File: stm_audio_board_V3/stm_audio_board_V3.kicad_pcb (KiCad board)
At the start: 4 copper layers, 201 x 117 mm, 258 parts, among them J1 Power conn, J10 USB_A, J11 AudioJack_Loop1_Return, J12 AudioJack_Loop1_Send, J13 AudioJack_INPUT_Main, J14 AudioJack_OUTPUT_Main, J15 AudioJack_Loop2_Send, J16 STlink_DISP_MCU, J2 STlink_DSP, J3 Audio_sig, J4 Conn_01x01_taptempo, J5 Barrel_Jack_MountingPin, J6 Conn_01x03_pot_ext, J7 AudioJack_Loop3_Return, J8 AudioJack_Loop3_Send, J9 AudioJack_Loop2_Return, SW1 SW_SPST, SW2 SW_SPST, U1 IS42S16100H-7TL, U10 OP275, U12 OP275, U13 LM7809_TO220, U14 OP275, U15 STM32H723ZGTx, U16 LM7909_TO220, U2 OP275, U3 R-78B5.0-2.0, U4 OP275, U5 MIC2920A-3.3WS-TR, U7 STM32H723ZGTx, U8 OP275, U9 MIC2920A-3.3WS-TR, Y1 X1E0000210132, Y2 X1E0000210132

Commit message: isolated power section done
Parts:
- removed C104, C105: 2u2F, Capacitor_SMD:C_0805_2012Metric_Pad1.18x1.45mm_HandSolder
- removed C132: 100uF, Capacitor_THT:CP_Radial_D6.3mm_P2.50mm
- removed D1: 1N4148, Diode_SMD:D_1206_3216Metric_Pad1.42x1.75mm_HandSolder
- removed FB4: TDK MMZ1608R601ATD25 DB, Resistor_SMD:R_0603_1608Metric_Pad0.98x0.95mm_HandSolder
- removed U3: R-78B5.0-2.0, Converter_DCDC:Converter_DCDC_RECOM_R-78B-2.0_THT
- added C103: 4.7uF, Capacitor_THT:CP_Radial_D6.3mm_P2.50mm, F.Cu at (295.6, 119.4)
- added C138: 100uF, Capacitor_THT:CP_Radial_D6.3mm_P2.50mm, F.Cu at (261.3, 108.5)
- added C139: 100uF, Capacitor_THT:CP_Radial_D6.3mm_P2.50mm, F.Cu at (253.0, 108.4)
- added C140: 47uF, Capacitor_THT:CP_Radial_D6.3mm_P2.50mm, F.Cu at (258.5, 140.5)
- added C48: 100uF, Capacitor_THT:CP_Radial_D6.3mm_P2.50mm, F.Cu at (288.9, 131.6)
- added C69: 100uF, Capacitor_THT:CP_Radial_D6.3mm_P2.50mm, F.Cu at (279.2, 131.4)
- added C75: 100uF, Capacitor_THT:CP_Radial_D6.3mm_P2.50mm, F.Cu at (300.9, 141.1)
- added C76: 100uF, Capacitor_THT:CP_Radial_D6.3mm_P2.50mm, F.Cu at (277.3, 140.6)
- added C77: 100uF, Capacitor_THT:CP_Radial_D6.3mm_P2.50mm, F.Cu at (269.3, 140.6)
- added L4: 10uH, Inductor_SMD:L_6.3x6.3_H3, F.Cu at (286.3, 142.1)
- added L5: 10uH, Inductor_SMD:L_6.3x6.3_H3, F.Cu at (238.2, 113.8)
- added PS1: URB2405S-6WR3, Converter_DCDC:Converter_DCDC_XP_POWER-ITxxxxxS_THT, F.Cu at (271.4, 132.4)
- C13: value 22uF 50V poly -> 100uF; footprint Capacitor_THT:CP_Radial_D5.0mm_P2.00mm -> Capacitor_THT:CP_Radial_D6.3mm_P2.50mm
- C133: value 47uF -> 4.7uF
- C15: value 2u2F -> 100uF; footprint Capacitor_SMD:C_0805_2012Metric_Pad1.18x1.45mm_HandSolder -> Capacitor_THT:CP_Radial_D6.3mm_P2.50mm
- C27: value 100n -> 100uF; footprint Capacitor_SMD:C_0603_1608Metric -> Capacitor_THT:CP_Radial_D6.3mm_P2.50mm
- C4: value 22uF tantal -> 100uF; footprint Capacitor_Tantalum_SMD:CP_EIA-7343-31_Kemet-D_Pad2.25x2.55mm_HandSolder -> Capacitor_THT:CP_Radial_D6.3mm_P2.50mm
- moved C9 44.3 mm to (194.4, 122.0), turned to 90 degrees
- moved C8 39.9 mm to (194.4, 113.9), turned to 90 degrees
- moved C13 39.3 mm to (293.9, 141.2), turned to -90 degrees
- moved J5 36.2 mm to (297.8, 132.7)
- moved C89 33.3 mm to (204.8, 70.7), turned to 0 degrees
- moved C27 31.9 mm to (254.4, 85.6), turned to 180 degrees
- moved C28 28.8 mm to (261.9, 85.6), turned to 0 degrees
- moved L1 23.7 mm to (287.3, 120.1), turned to 180 degrees
- moved C133 21.9 mm to (278.9, 119.3)
- moved C15 21.4 mm to (234.4, 104.4)
- moved C30 20.9 mm to (209.8, 87.0)
- moved C102 19.0 mm to (243.0, 113.1), turned to 0 degrees
- moved C4 17.9 mm to (245.4, 116.6), turned to -90 degrees
- moved C70 15.6 mm to (241.2, 126.1), turned to -90 degrees
- moved C119 14.4 mm to (260.8, 56.4), turned to 0 degrees
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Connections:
- C13 pad 2: GND -> Earth
- C133 pad 2: GND -> Earth
- C15 pad 1: 5V -> Net-(U5-VI)
- C27 pad 1: Net-(U5-VI) -> GND
- C27 pad 2: GND -> -9V
- C28 pad 1: Net-(U5-VI) -> +9V
- J5 pad 2: GND -> Earth
- PS2 pad 1: GND -> Earth
- U13 pad 3: unconnected-(U13-VO-Pad3) -> +9V
- U16 pad 3: unconnected-(U16-VO-Pad3) -> -9V
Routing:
- net +9V: track 245.3 -> 196.8 mm, vias 6 -> 5
- net ADC1N: track 43.5 -> 6.32 mm
- net ADC1P: track 43.1 -> 6.15 mm
- net GND: track 90.7 -> 117.4 mm
- net AD1939_CM: track 216.2 -> 197.1 mm, vias 12 -> 10
- net Audio_Main_Input: track 12.2 -> 6.80 mm
- added copper zone on In1.Cu, net Earth
- added copper zone on In2.Cu, net Earth
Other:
- board size 201 x 117 mm -> 236.9 x 117.5 mm

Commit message: minor power section fixes
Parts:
- added C104: 10uF, Capacitor_SMD:C_1206_3216Metric, F.Cu at (285.7, 142.7)
- added C105: 10uF, Capacitor_SMD:C_1206_3216Metric, F.Cu at (283.1, 142.7)
- added C132: 10uF, Capacitor_SMD:C_1206_3216Metric, F.Cu at (272.6, 142.7)
- added C136: 10uF, Capacitor_SMD:C_1206_3216Metric, F.Cu at (270.0, 142.7)
- added C137: 10uF, Capacitor_SMD:C_1206_3216Metric, F.Cu at (286.3, 119.1)
- added C141: 10uF, Capacitor_SMD:C_1206_3216Metric, F.Cu at (324.3, 105.5)
- added C142: 10uF, Capacitor_SMD:C_1206_3216Metric, F.Cu at (324.3, 108.9)
- added C143: 10uF, Capacitor_SMD:C_1206_3216Metric, F.Cu at (324.3, 112.2)
- added C144: 10uF, Capacitor_SMD:C_1206_3216Metric, F.Cu at (329.9, 95.5)
- added C145: 10uF, Capacitor_SMD:C_1206_3216Metric, F.Cu at (329.9, 98.8)
- added C146: 10uF, Capacitor_SMD:C_1206_3216Metric, F.Cu at (329.9, 102.2)
- added C147: 10uF, Capacitor_SMD:C_1206_3216Metric, F.Cu at (329.9, 105.5)
- added C148: 10uF, Capacitor_SMD:C_1206_3216Metric, F.Cu at (237.3, 142.0)
- added C149: 10uF, Capacitor_SMD:C_1206_3216Metric, F.Cu at (242.7, 142.1)
- added C150: 100uF, Capacitor_THT:CP_Radial_D6.3mm_P2.50mm, F.Cu at (232.0, 128.9)
- added C151: 100uF, Capacitor_THT:CP_Radial_D6.3mm_P2.50mm, F.Cu at (232.1, 143.2)
- added C152: 10uF, Capacitor_SMD:C_1206_3216Metric, F.Cu at (322.6, 89.8)
- added C153: 10uF, Capacitor_SMD:C_1206_3216Metric, F.Cu at (322.6, 93.1)
- added C154: 10uF, Capacitor_SMD:C_1206_3216Metric, F.Cu at (322.6, 96.5)
- added C155: 10uF, Capacitor_SMD:C_1206_3216Metric, F.Cu at (322.6, 99.8)
- added L6: 10uH, Inductor_SMD:L_6.3x6.3_H3, F.Cu at (239.9, 136.0)
- C103, C133: value 4.7uF -> 10uF; footprint Capacitor_THT:CP_Radial_D6.3mm_P2.50mm -> Capacitor_SMD:C_1206_3216Metric
- C138, C139: value 100uF -> 10uF; footprint Capacitor_THT:CP_Radial_D6.3mm_P2.50mm -> Capacitor_SMD:C_1206_3216Metric
- C140: value 47uF -> 100uF
- moved C139 71.5 mm to (324.3, 102.2)
- moved H4 54.9 mm to (291.8, 71.6)
- moved C140 26.9 mm to (232.0, 136.0)
- moved C75 21.7 mm to (284.3, 127.2), turned to 90 degrees
- moved C4 17.9 mm to (237.9, 100.3)
- moved L5 17.9 mm to (230.7, 97.5)
- moved C13 17.6 mm to (279.8, 130.6), turned to 180 degrees
- moved C70 16.7 mm to (229.7, 114.0)
- moved C15 16.5 mm to (237.1, 88.1)
- moved C29 15.4 mm to (237.7, 79.5)
- moved C138 13.7 mm to (272.2, 116.8), turned to -90 degrees
- moved C76 13.6 mm to (269.7, 129.4), turned to 90 degrees
- moved C77 13.5 mm to (261.8, 129.4), turned to 90 degrees
- moved C103 12.1 mm to (283.5, 119.1), turned to 90 degrees
- moved C102 11.3 mm to (233.8, 106.6)
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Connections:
- C138 pad 1: Net-(U13-VI) -> Net-(PS2-+Vin)
- C138 pad 2: GND -> Earth
- C139 pad 1: GND -> Net-(U16-VI)
- C139 pad 2: Net-(U16-VI) -> GND
- PS1 pad 6: 5V -> Net-(PS1-+Vout)
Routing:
- net 5V: track 0.00 -> 32.3 mm
- net PWR_INPUT_12V-18V: track 0.00 -> 19.1 mm
- net Net-(PS1-+Vout): track 0.00 -> 16.3 mm
- net Net-(PS2-+Vin): track 0.00 -> 15.9 mm
- net Net-(PS1-+Vin): track 0.00 -> 9.46 mm
- net Earth: vias 0 -> 25
- added copper zone on F.Cu, net Earth
- added copper zone on F.Cu, net Net-(PS1-+Vin)
- added copper zone on F.Cu, net PWR_INPUT_12V-18V
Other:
- board size 236.9 x 117.5 mm -> 230.9 x 117 mm

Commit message: safety commit
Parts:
- moved C145 81.8 mm to (249.2, 86.1), turned to 180 degrees
- moved C144 81.0 mm to (249.2, 88.6), turned to 180 degrees
- moved C141 80.5 mm to (243.8, 105.9), turned to -90 degrees
- moved C139 78.0 mm to (246.4, 105.9), turned to -90 degrees
- moved C154 74.4 mm to (248.9, 105.9), turned to -90 degrees
- moved C147 70.4 mm to (261.5, 88.7)
- moved C146 70.2 mm to (261.5, 86.3)
- moved C155 69.1 mm to (254.4, 88.6)
- moved C143 59.3 mm to (265.3, 106.0), turned to -90 degrees
- moved C142 56.5 mm to (267.8, 106.0), turned to -90 degrees
- moved C153 56.2 mm to (266.6, 88.7), turned to 180 degrees
- moved C152 54.7 mm to (270.3, 106.0), turned to -90 degrees
- moved C27 4.70 mm to (254.3, 80.9)
- moved C28 4.65 mm to (261.2, 81.0)
- moved C134 0.22 mm to (269.3, 99.8)
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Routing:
- net Net-(U16-VI): track 0.00 -> 26.3 mm
- net Net-(U13-VI): track 0.00 -> 25.9 mm
- net /Power/-12V: track 0.00 -> 23.6 mm
- net /Power/+12V: track 0.00 -> 22.8 mm
- net GND: track 117.4 -> 133.7 mm, vias 56 -> 85
- net -9V: track 225.8 -> 237.0 mm
- net +9V: track 196.8 -> 206.1 mm
- added copper zone on F.Cu, net GND
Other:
- board text added: "POWER INPUT 18V"

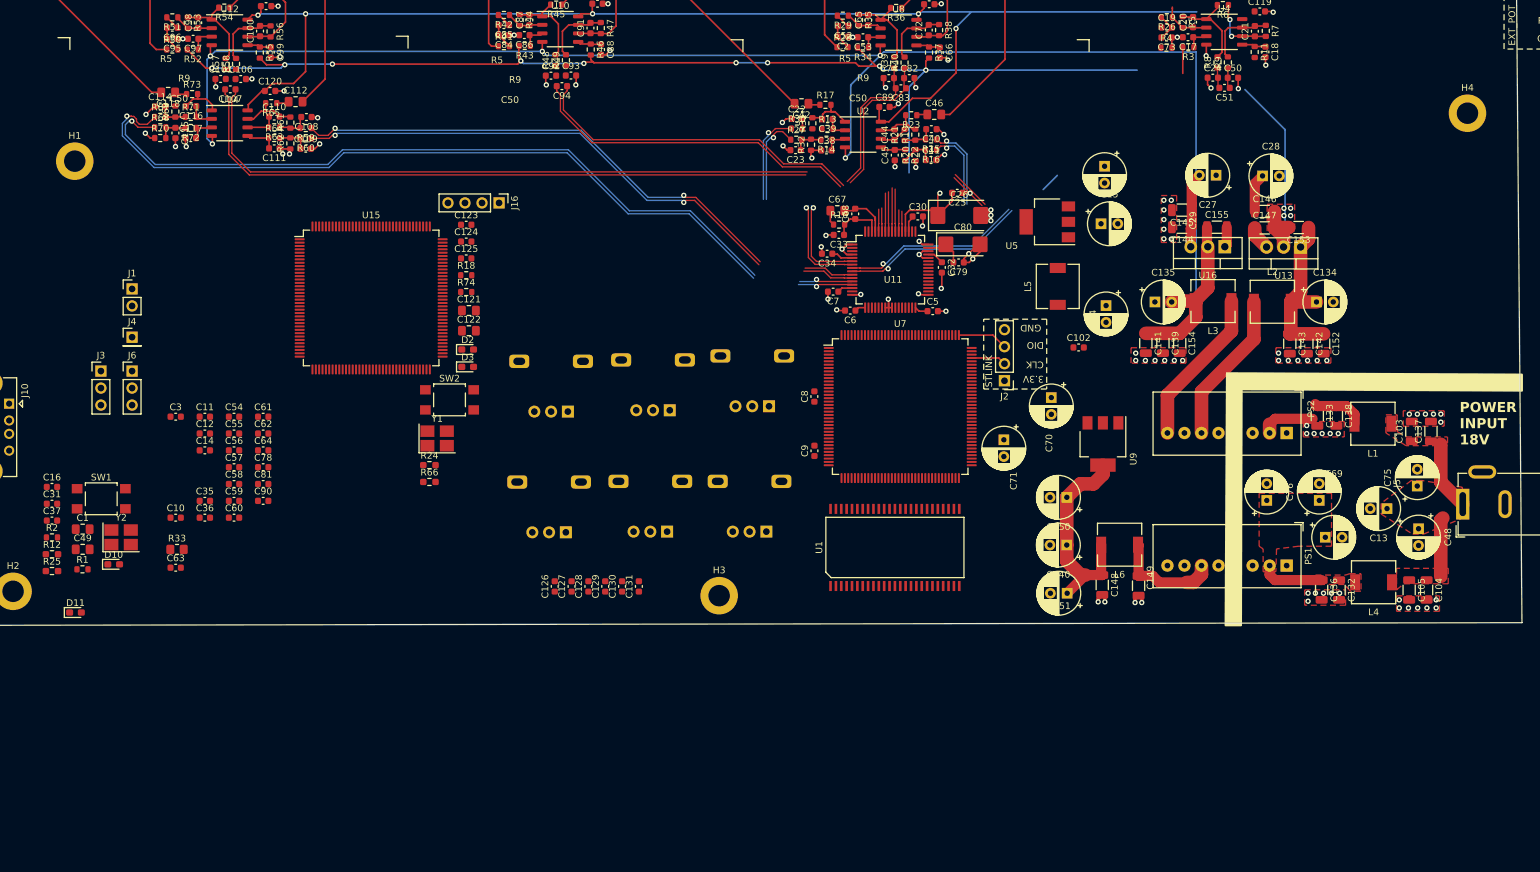
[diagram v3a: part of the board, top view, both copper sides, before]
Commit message: Analog power and SDRAm routing reworked
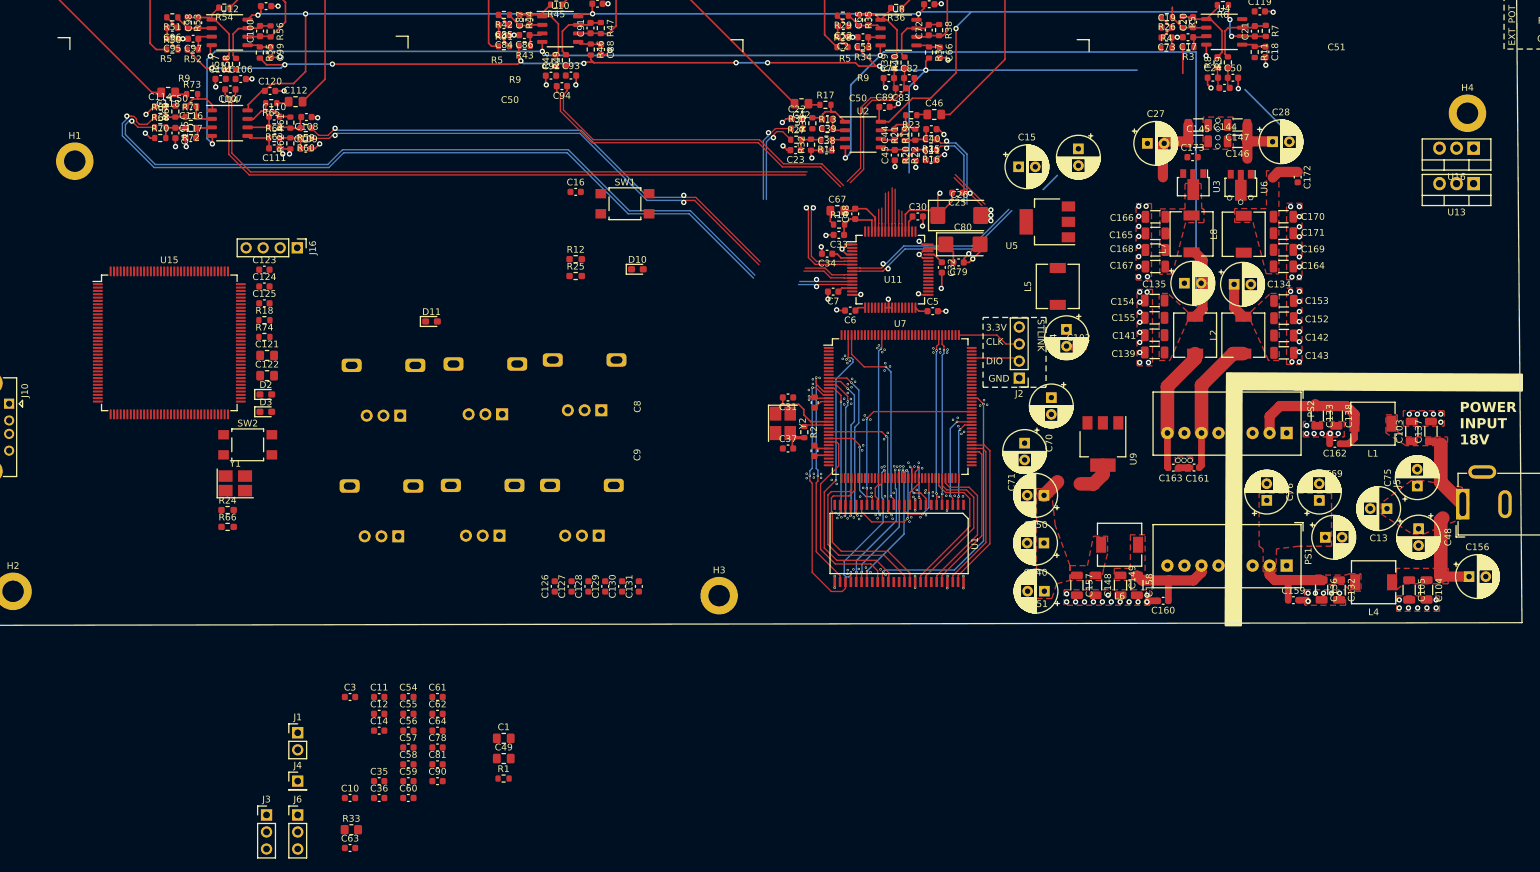
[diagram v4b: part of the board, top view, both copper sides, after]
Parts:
- added C156: 100uF, Capacitor_THT:CP_Radial_D6.3mm_P2.50mm, F.Cu at (292.0, 140.7)
- added C157: 10uF, Capacitor_SMD:C_1206_3216Metric, F.Cu at (233.5, 142.0)
- added C158: 10uF, Capacitor_SMD:C_1206_3216Metric, F.Cu at (242.5, 142.0)
- added C159: 100nF, Capacitor_SMD:C_0603_1608Metric, F.Cu at (265.8, 144.2)
- added C160: 100nF, Capacitor_SMD:C_0603_1608Metric, F.Cu at (246.4, 144.3)
- added C161: 100nF, Capacitor_SMD:C_0603_1608Metric, F.Cu at (251.0, 124.5)
- added C162: 100nF, Capacitor_SMD:C_0603_1608Metric, F.Cu at (272.0, 120.9)
- added C163: 100nF, Capacitor_SMD:C_0603_1608Metric, F.Cu at (247.9, 124.5)
- added C164: 10uF, Capacitor_SMD:C_1206_3216Metric, F.Cu at (264.3, 94.5)
- added C165: 10uF, Capacitor_SMD:C_1206_3216Metric, F.Cu at (245.2, 89.5)
- added C166: 10uF, Capacitor_SMD:C_1206_3216Metric, F.Cu at (245.2, 87.1)
- added C167: 10uF, Capacitor_SMD:C_1206_3216Metric, F.Cu at (245.2, 94.5)
- added C168: 10uF, Capacitor_SMD:C_1206_3216Metric, F.Cu at (245.2, 92.0)
- added C169: 10uF, Capacitor_SMD:C_1206_3216Metric, F.Cu at (264.3, 92.0)
- added C170: 10uF, Capacitor_SMD:C_1206_3216Metric, F.Cu at (264.3, 87.1)
- added C171: 10uF, Capacitor_SMD:C_1206_3216Metric, F.Cu at (264.3, 89.5)
- added C172: 100nF, Capacitor_SMD:C_0603_1608Metric, F.Cu at (266.5, 81.2)
- added C173: 100nF, Capacitor_SMD:C_0603_1608Metric, F.Cu at (250.8, 78.2)
- added L7: 10uH, Inductor_SMD:L_6.3x6.3_H3, F.Cu at (250.6, 89.6)
- added L8: 10uH, Inductor_SMD:L_6.3x6.3_H3, F.Cu at (258.4, 89.7)
- added U3: 7909, Package_TO_SOT_SMD:SOT-89-3, F.Cu at (250.9, 82.6)
- added U6: 7809, Package_TO_SOT_SMD:SOT-89-3, F.Cu at (258.0, 82.7)
- moved R2 113.3 mm to (192.9, 119.2), turned to -90 degrees
- moved C31 110.9 mm to (190.4, 114.0), turned to 180 degrees
- moved C37 110.3 mm to (190.4, 121.6)
- moved Y2 100.2 mm to (189.7, 117.9), turned to -90 degrees
- moved R12 89.6 mm to (158.8, 93.4)
- moved C16 89.6 mm to (158.8, 83.4)
- moved D10 89.6 mm to (168.0, 94.9)
- moved R25 89.6 mm to (158.8, 95.9)
- moved SW1 89.6 mm to (166.1, 85.1)
- moved J1 70.7 mm to (117.3, 164.0)
- moved J3 70.7 mm to (112.7, 176.3)
- moved J6 70.7 mm to (117.3, 176.3)
- moved J4 70.7 mm to (117.3, 171.2)
- moved C49 70.1 mm to (148.1, 167.9)
- moved C1 70.1 mm to (148.1, 164.9)
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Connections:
- C134 pad 1: Net-(U13-VI) -> Net-(C134-Pad1)
- C135 pad 2: Net-(U16-VI) -> Net-(C135-Pad2)
- C139 pad 1: Net-(U16-VI) -> Net-(C135-Pad2)
- C141 pad 1: Net-(U16-VI) -> Net-(C135-Pad2)
- C142 pad 1: Net-(U13-VI) -> Net-(C134-Pad1)
- C143 pad 1: Net-(U13-VI) -> Net-(C134-Pad1)
- C152 pad 1: Net-(U13-VI) -> Net-(C134-Pad1)
- C153 pad 1: Net-(U13-VI) -> Net-(C134-Pad1)
- C154 pad 1: Net-(U16-VI) -> Net-(C135-Pad2)
- C155 pad 1: Net-(U16-VI) -> Net-(C135-Pad2)
- L2 pad 2: Net-(U13-VI) -> Net-(C134-Pad1)
- L3 pad 2: Net-(U16-VI) -> Net-(C135-Pad2)
- U1 pad 1: unconnected-(U1B-VDD-Pad1) -> +3.3V
- U1 pad 10: unconnected-(U1B-GNDQ-Pad10) -> GND
- U1 pad 11: unconnected-(U1A-DQ6-Pad11) -> /MCU/DSP_SDRAM_DATA_BUS6
- U1 pad 12: unconnected-(U1A-DQ7-Pad12) -> /MCU/DSP_SDRAM_DATA_BUS7
- U1 pad 13: unconnected-(U1B-VDDQ-Pad13) -> +3.3V
- U1 pad 14: unconnected-(U1A-LDQM-Pad14) -> /MCU/DSP_SDRAM_LDQM
- U1 pad 15: unconnected-(U1A-/WE-Pad15) -> /MCU/DSP_SDRAM_WE
- U1 pad 16: unconnected-(U1A-/CAS-Pad16) -> /MCU/DSP_SDRAM_CAS
- U1 pad 17: unconnected-(U1A-/RAS-Pad17) -> /MCU/DSP_SDRAM_RAS
- U1 pad 18: unconnected-(U1A-/CS-Pad18) -> /MCU/DSP_SDRAM_CS
- U1 pad 19: unconnected-(U1A-A11-Pad19) -> /MCU/DSP_SDRAM_ADRESS_BUS11
- U1 pad 2: unconnected-(U1A-DQ0-Pad2) -> /MCU/DSP_SDRAM_DATA_BUS0
- U1 pad 20: unconnected-(U1A-A10-Pad20) -> /MCU/DSP_SDRAM_ADRESS_BUS10
- U1 pad 21: unconnected-(U1A-A0-Pad21) -> /MCU/DSP_SDRAM_ADRESS_BUS0
- U1 pad 22: unconnected-(U1A-A1-Pad22) -> /MCU/DSP_SDRAM_ADRESS_BUS1
- U1 pad 23: unconnected-(U1A-A2-Pad23) -> /MCU/DSP_SDRAM_ADRESS_BUS2
- U1 pad 24: unconnected-(U1A-A3-Pad24) -> /MCU/DSP_SDRAM_ADRESS_BUS3
- U1 pad 25: unconnected-(U1B-VDD-Pad25) -> +3.3V
- U1 pad 26: unconnected-(U1B-GND-Pad26) -> GND
- U1 pad 27: unconnected-(U1A-A4-Pad27) -> /MCU/DSP_SDRAM_ADRESS_BUS4
- U1 pad 28: unconnected-(U1A-A5-Pad28) -> /MCU/DSP_SDRAM_ADRESS_BUS5
- U1 pad 29: unconnected-(U1A-A6-Pad29) -> /MCU/DSP_SDRAM_ADRESS_BUS6
- U1 pad 3: unconnected-(U1A-DQ1-Pad3) -> /MCU/DSP_SDRAM_DATA_BUS1
- U1 pad 30: unconnected-(U1A-A7-Pad30) -> /MCU/DSP_SDRAM_ADRESS_BUS7
- U1 pad 31: unconnected-(U1A-A8-Pad31) -> /MCU/DSP_SDRAM_ADRESS_BUS8
- U1 pad 32: unconnected-(U1A-A9-Pad32) -> /MCU/DSP_SDRAM_ADRESS_BUS9
- U1 pad 34: unconnected-(U1A-CKE-Pad34) -> /MCU/DSP_SDRAM_CKE
- U1 pad 35: unconnected-(U1A-CLK-Pad35) -> /MCU/DSP_SDRAM_CLK
- U1 pad 36: unconnected-(U1A-UDQM-Pad36) -> /MCU/DSP_SDRAM_UDQM
- U1 pad 38: unconnected-(U1B-VDDQ-Pad38) -> +3.3V
- U1 pad 39: unconnected-(U1A-DQ8-Pad39) -> /MCU/DSP_SDRAM_DATA_BUS8
- U1 pad 4: unconnected-(U1B-GNDQ-Pad4) -> GND
- U1 pad 40: unconnected-(U1A-DQ9-Pad40) -> /MCU/DSP_SDRAM_DATA_BUS9
- U1 pad 41: unconnected-(U1B-GNDQ-Pad41) -> GND
- U1 pad 42: unconnected-(U1A-DQ10-Pad42) -> /MCU/DSP_SDRAM_DATA_BUS10
- U1 pad 43: unconnected-(U1A-DQ11-Pad43) -> /MCU/DSP_SDRAM_DATA_BUS11
- U1 pad 44: unconnected-(U1B-VDDQ-Pad44) -> +3.3V
- U1 pad 45: unconnected-(U1A-DQ12-Pad45) -> /MCU/DSP_SDRAM_DATA_BUS12
- U1 pad 46: unconnected-(U1A-DQ13-Pad46) -> /MCU/DSP_SDRAM_DATA_BUS13
- U1 pad 47: unconnected-(U1B-GNDQ-Pad47) -> GND
- U1 pad 48: unconnected-(U1A-DQ14-Pad48) -> /MCU/DSP_SDRAM_DATA_BUS14
- U1 pad 49: unconnected-(U1A-DQ15-Pad49) -> /MCU/DSP_SDRAM_DATA_BUS15
- U1 pad 5: unconnected-(U1A-DQ2-Pad5) -> /MCU/DSP_SDRAM_DATA_BUS2
- U1 pad 50: unconnected-(U1B-GND-Pad50) -> GND
- U1 pad 6: unconnected-(U1A-DQ3-Pad6) -> /MCU/DSP_SDRAM_DATA_BUS3
- U1 pad 7: unconnected-(U1B-VDDQ-Pad7) -> +3.3V
- U1 pad 8: unconnected-(U1A-DQ4-Pad8) -> /MCU/DSP_SDRAM_DATA_BUS4
- U1 pad 9: unconnected-(U1A-DQ5-Pad9) -> /MCU/DSP_SDRAM_DATA_BUS5
- U13 pad 1: Net-(U13-VI) -> unconnected-(U13-VI-Pad1)
- U13 pad 3: +9V -> unconnected-(U13-VO-Pad3)
- U16 pad 2: Net-(U16-VI) -> unconnected-(U16-VI-Pad2)
- U16 pad 3: -9V -> unconnected-(U16-VO-Pad3)
- U7 pad 10: unconnected-(U7-PF0-Pad10) -> /MCU/DSP_SDRAM_ADRESS_BUS0
- U7 pad 11: unconnected-(U7-PF1-Pad11) -> /MCU/DSP_SDRAM_ADRESS_BUS1
- U7 pad 114: unconnected-(U7-PD0-Pad114) -> /MCU/DSP_SDRAM_DATA_BUS2
- U7 pad 115: unconnected-(U7-PD1-Pad115) -> /MCU/DSP_SDRAM_DATA_BUS3
- U7 pad 12: unconnected-(U7-PF2-Pad12) -> /MCU/DSP_SDRAM_ADRESS_BUS2
- U7 pad 13: unconnected-(U7-PF3-Pad13) -> /MCU/DSP_SDRAM_ADRESS_BUS3
- U7 pad 132: unconnected-(U7-PG15-Pad132) -> /MCU/DSP_SDRAM_CAS
- U7 pad 14: unconnected-(U7-PF4-Pad14) -> /MCU/DSP_SDRAM_ADRESS_BUS4
- U7 pad 141: unconnected-(U7-PE0-Pad141) -> /MCU/DSP_SDRAM_LDQM
- U7 pad 142: unconnected-(U7-PE1-Pad142) -> /MCU/DSP_SDRAM_UDQM
- U7 pad 15: unconnected-(U7-PF5-Pad15) -> /MCU/DSP_SDRAM_ADRESS_BUS5
- U7 pad 26: unconnected-(U7-PC0-Pad26) -> /MCU/DSP_SDRAM_WE
- U7 pad 28: unconnected-(U7-PC2_C-Pad28) -> /MCU/DSP_SDRAM_CS
- U7 pad 29: unconnected-(U7-PC3_C-Pad29) -> /MCU/DSP_SDRAM_CKE
- U7 pad 40: unconnected-(U7-PA4-Pad40) -> /MCU/DSP_SDRAM_DATA_BUS8
- U7 pad 41: unconnected-(U7-PA5-Pad41) -> /MCU/DSP_SDRAM_DATA_BUS9
- U7 pad 49: unconnected-(U7-PF11-Pad49) -> /MCU/DSP_SDRAM_RAS
- U7 pad 50: unconnected-(U7-PF12-Pad50) -> /MCU/DSP_SDRAM_ADRESS_BUS6
- U7 pad 53: unconnected-(U7-PF13-Pad53) -> /MCU/DSP_SDRAM_ADRESS_BUS7
- U7 pad 54: unconnected-(U7-PF14-Pad54) -> /MCU/DSP_SDRAM_ADRESS_BUS8
- U7 pad 55: unconnected-(U7-PF15-Pad55) -> /MCU/DSP_SDRAM_ADRESS_BUS9
- U7 pad 56: unconnected-(U7-PG0-Pad56) -> /MCU/DSP_SDRAM_ADRESS_BUS10
- U7 pad 58: unconnected-(U7-PE7-Pad58) -> /MCU/DSP_SDRAM_DATA_BUS4
- U7 pad 59: unconnected-(U7-PE8-Pad59) -> /MCU/DSP_SDRAM_DATA_BUS5
- U7 pad 60: unconnected-(U7-PE9-Pad60) -> /MCU/DSP_SDRAM_DATA_BUS6
- U7 pad 63: unconnected-(U7-PE10-Pad63) -> /MCU/DSP_SDRAM_DATA_BUS7
- U7 pad 66: unconnected-(U7-PE13-Pad66) -> /MCU/DSP_SDRAM_DATA_BUS10
- U7 pad 67: unconnected-(U7-PE14-Pad67) -> /MCU/DSP_SDRAM_DATA_BUS11
- U7 pad 68: unconnected-(U7-PE15-Pad68) -> /MCU/DSP_SDRAM_DATA_BUS12
- U7 pad 77: unconnected-(U7-PD8-Pad77) -> /MCU/DSP_SDRAM_DATA_BUS13
- U7 pad 78: unconnected-(U7-PD9-Pad78) -> /MCU/DSP_SDRAM_DATA_BUS14
- U7 pad 79: unconnected-(U7-PD10-Pad79) -> /MCU/DSP_SDRAM_DATA_BUS15
- U7 pad 85: unconnected-(U7-PD14-Pad85) -> /MCU/DSP_SDRAM_DATA_BUS0
- U7 pad 86: unconnected-(U7-PD15-Pad86) -> /MCU/DSP_SDRAM_DATA_BUS1
- U7 pad 89: unconnected-(U7-PG4-Pad89) -> /MCU/DSP_SDRAM_ADRESS_BUS11
- U7 pad 93: unconnected-(U7-PG8-Pad93) -> /MCU/DSP_SDRAM_CLK
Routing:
- net /MCU/DSP_SDRAM_UDQM: track 0.00 -> 47.4 mm, vias 0 -> 2
- net /MCU/DSP_SDRAM_CLK: track 0.00 -> 41.0 mm, vias 0 -> 2
- net /MCU/DSP_SDRAM_ADRESS_BUS5: track 0.00 -> 38.0 mm, vias 0 -> 2
- net /MCU/DSP_SDRAM_ADRESS_BUS4: track 0.00 -> 35.5 mm, vias 0 -> 2
- net /MCU/DSP_SDRAM_CKE: track 0.00 -> 30.0 mm
- net /MCU/DSP_SDRAM_LDQM: track 0.00 -> 29.9 mm, vias 0 -> 2
- net /MCU/DSP_SDRAM_ADRESS_BUS11: track 0.00 -> 29.0 mm, vias 0 -> 2
- net /MCU/DSP_SDRAM_CAS: track 0.00 -> 28.8 mm, vias 0 -> 2
- net /MCU/DSP_SDRAM_DATA_BUS9: track 0.00 -> 27.3 mm
- net /MCU/DSP_SDRAM_DATA_BUS8: track 0.00 -> 27.3 mm
- net Net-(U16-VI): track 26.3 -> 0.00 mm
- net /MCU/DSP_SDRAM_ADRESS_BUS0: track 0.00 -> 26.0 mm, vias 0 -> 2
- net Net-(U13-VI): track 25.9 -> 0.00 mm
- net /MCU/DSP_SDRAM_DATA_BUS2: track 0.00 -> 25.6 mm, vias 0 -> 2
- net /MCU/DSP_SDRAM_DATA_BUS3: track 0.00 -> 25.5 mm, vias 0 -> 2
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- added copper zone on F.Cu, net 5V
- added copper zone on F.Cu, net Net-(C134-Pad1)
- added copper zone on F.Cu, net Net-(C135-Pad2)
- added copper zone on F.Cu, net Net-(PS1-+Vout)
- added copper zone on F.Cu, net Net-(U3-VI)
- added copper zone on F.Cu, net unconnected-(U13-VI-Pad1)
